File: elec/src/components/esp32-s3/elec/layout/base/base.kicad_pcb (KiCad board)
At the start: 2 copper layers, 38 parts, among them U1 ?, U2 ?, U3 ?, U4 ?, U5 ?, U6 ?, U7 ?, U8 ?, U9 ?

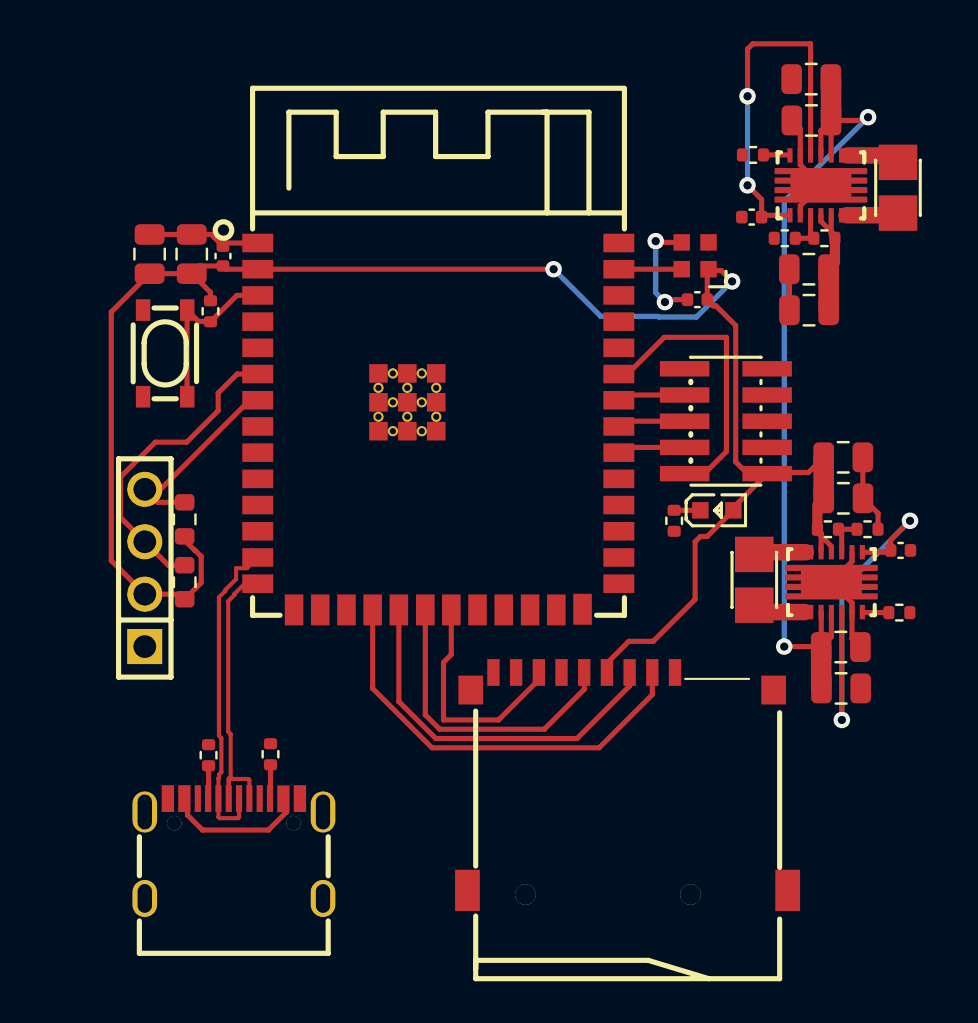
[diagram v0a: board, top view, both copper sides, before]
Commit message: Layout controller block
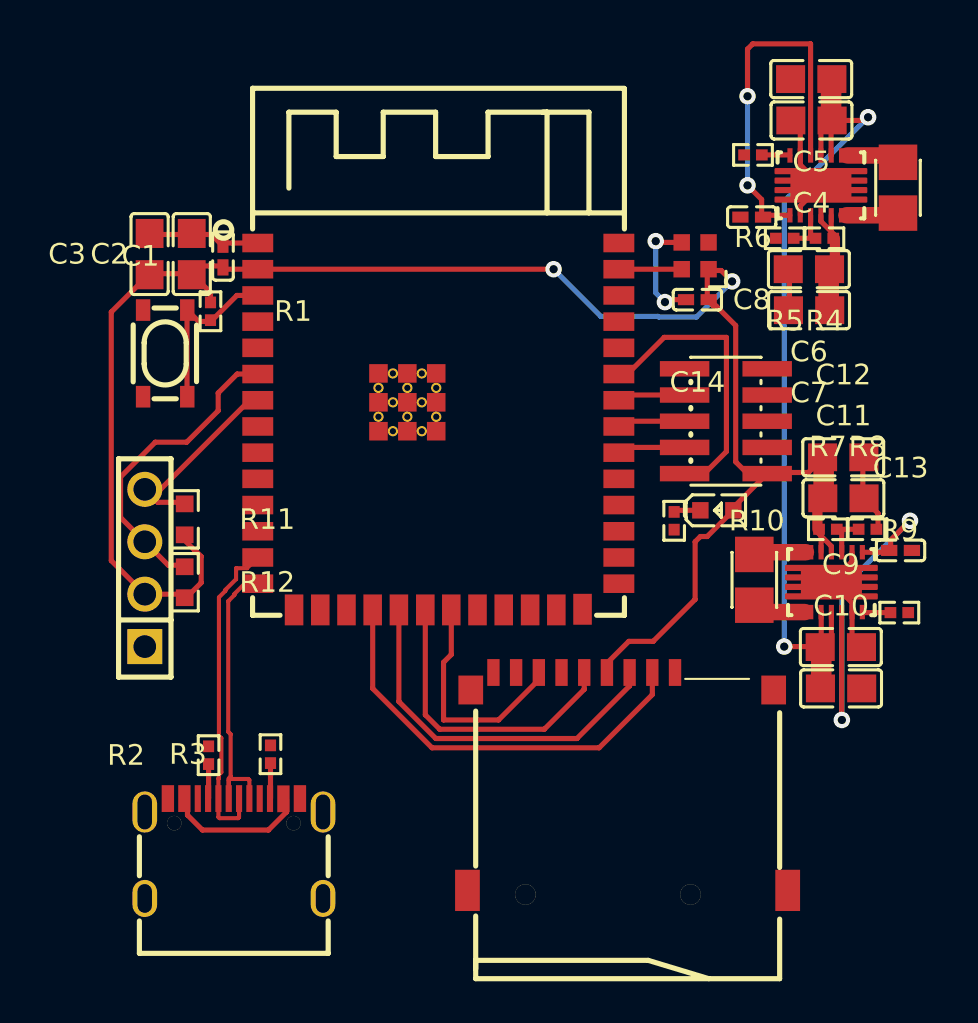
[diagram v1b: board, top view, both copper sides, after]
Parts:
- C1, C13, C14, C8: value 16V 100nF X7R ±10% 0402 Multilayer Ceramic Capacitors MLCC - SMD/SMT ROHS -> 100nF ±10% 16V X7R; footprint lib:C0402 -> atopile:C0402-b3ef17
- C10, C11, C12, C2, C3, C4, C5, C6, C7, C9: value 25V 10uF X5R ±10% 0805 Multilayer Ceramic Capacitors MLCC - SMD/SMT ROHS -> 10µF ±10% 25V X5R; footprint lib:C0805 -> atopile:C0805-3b2e55
- L1, L2, LED1, U1, U2, U3, U4, U5, U6, U7, U8, U9: value ? -> (none)
- R1: value 62.5mW Thick Film Resistors 50V ±100ppm/℃ ±1% 10kΩ 0402 Chip Resistor - Surface Mount ROHS -> 10kΩ ±1% 62.5mW; footprint lib:R0402 -> atopile:R0402-56259e
- R10: value 62.5mW Thick Film Resistors 50V ±100ppm/℃ ±1% 330Ω 0402 Chip Resistor - Surface Mount ROHS -> 1kΩ ±1% 62.5mW; footprint lib:R0402 -> atopile:R0402-56259e
- R11, R12: value 100mW Thick Film Resistors 75V ±100ppm/℃ ±1% 2.7kΩ 0603 Chip Resistor - Surface Mount ROHS -> 2.7kΩ ±1% 100mW; footprint lib:R0603 -> atopile:R0603-ebcab9
- R2, R3: value 62.5mW Thick Film Resistors 50V ±100ppm/℃ ±1% 4.7kΩ 0402 Chip Resistor - Surface Mount ROHS -> 4.7kΩ ±1% 62.5mW; footprint lib:R0402 -> atopile:R0402-56259e
- R4: value 62.5mW 50V ±100ppm/℃ ±1% 25.5kΩ 0402 Chip Resistor - Surface Mount ROHS -> 1kΩ ±1% 62.5mW; footprint lib:R0402 -> atopile:R0402-56259e
- R5: value 62.5mW Thick Film Resistors 50V ±1% ±200ppm/℃ 2.8kΩ 0402 Chip Resistor - Surface Mount ROHS -> 1kΩ ±1% 62.5mW; footprint lib:R0402 -> atopile:R0402-56259e
- R6, R9: value 62.5mW Thick Film Resistors 50V ±100ppm/℃ ±1% 1MΩ 0402 Chip Resistor - Surface Mount ROHS -> 1MΩ ±1% 62.5mW; footprint lib:R0402 -> atopile:R0402-56259e
- R7: value 62.5mW Thick Film Resistors 50V ±100ppm/℃ ±1% 23.7kΩ 0402 Chip Resistor - Surface Mount ROHS -> 1kΩ ±1% 62.5mW; footprint lib:R0402 -> atopile:R0402-56259e
- R8: value 62.5mW Thick Film Resistors 50V ±100ppm/℃ ±1% 4.3kΩ 0402 Chip Resistor - Surface Mount ROHS -> 1kΩ ±1% 62.5mW; footprint lib:R0402 -> atopile:R0402-56259e
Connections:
- net _3v3_reg.feedback_div-out renamed _3v3_reg-out
- net _3v3_reg.ic-l1 renamed L1
- net _3v3_reg.ic-l2 renamed L2-1
- net _3v3_reg.ic-pg renamed _3v3_reg-PG
- net _3v3_reg.ic-vina renamed VINA
- net _5v_reg-vcc renamed hv-2
- net _5v_reg.feedback_div-out renamed _5v_reg-out
- net _5v_reg.ic-l1 renamed L1-1
- net _5v_reg.ic-l2 renamed L2
- net _5v_reg.ic-pg renamed _5v_reg-PG
- net _5v_reg.ic-vina renamed EN
- net cc1 renamed CC1
- net cc2 renamed B5
- net cd renamed CD
- net dat1_rsv_ renamed DAT1_RSV_
- net dat2_rsv_ renamed DAT2_RSV_
- net en renamed in
- net io1 renamed io
- net rxd0 renamed RXD0
- net scl renamed line-1
- net sda renamed line
- net sub1 renamed A8
- net sub2 renamed B8
- net txd0 renamed TXD0
- net uc.ic-gnd renamed gnd
- net uc.ic-vcc renamed hv
- net usb_conn-vcc renamed VBUS
- net vcc renamed hv-1
- U3 pad 10: reset -> (no net)
